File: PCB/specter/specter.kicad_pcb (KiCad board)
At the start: 4 copper layers, 65 x 84.5 mm, 114 parts, among them J1 USB_C_Receptacle_USB2.0_16P, J10 Conn_01x01, J11 Conn_01x01, J13 Conn_01x01, J14 Conn_01x01, J16 Conn_01x01, J17 Conn_01x01, J18 Conn_01x01, J19 Conn_01x01, J2 Micro_SD_Card_Det2, J22 SM04B-SRSS-TB_LF__SN_, J23 Conn_01x01, J24 SM04B-SRSS-TB_LF__SN_, J25 SM04B-SRSS-TB_LF__SN_, J26 SM04B-SRSS-TB_LF__SN_, J27 SM06B-SRSS-TB_LF__SN_, J28 SM06B-SRSS-TB_LF__SN_, J29 SM06B-SRSS-TB_LF__SN_, J3 Bus_M.2_Socket_M, J30 SM06B-SRSS-TB_LF__SN_, J4 Conn_01x22_Socket, J5 Conn_01x22_Socket, J6 Conn_02x01, J7 Conn_01x03, J8 Conn_01x01, J9 Conn_02x01, U1 FT232RL, U10 ASEK-32.768KHZ-L-R-T, U2 FT232RL, U3 RT9742GGJ5, U4 MagJack-A70-112-331N126, U5 TPD4EUSB30, U6 TPD4EUSB30, U7 74LVC1G07_copy, U8 AP2553W6, U9 AP3441SHE-7B

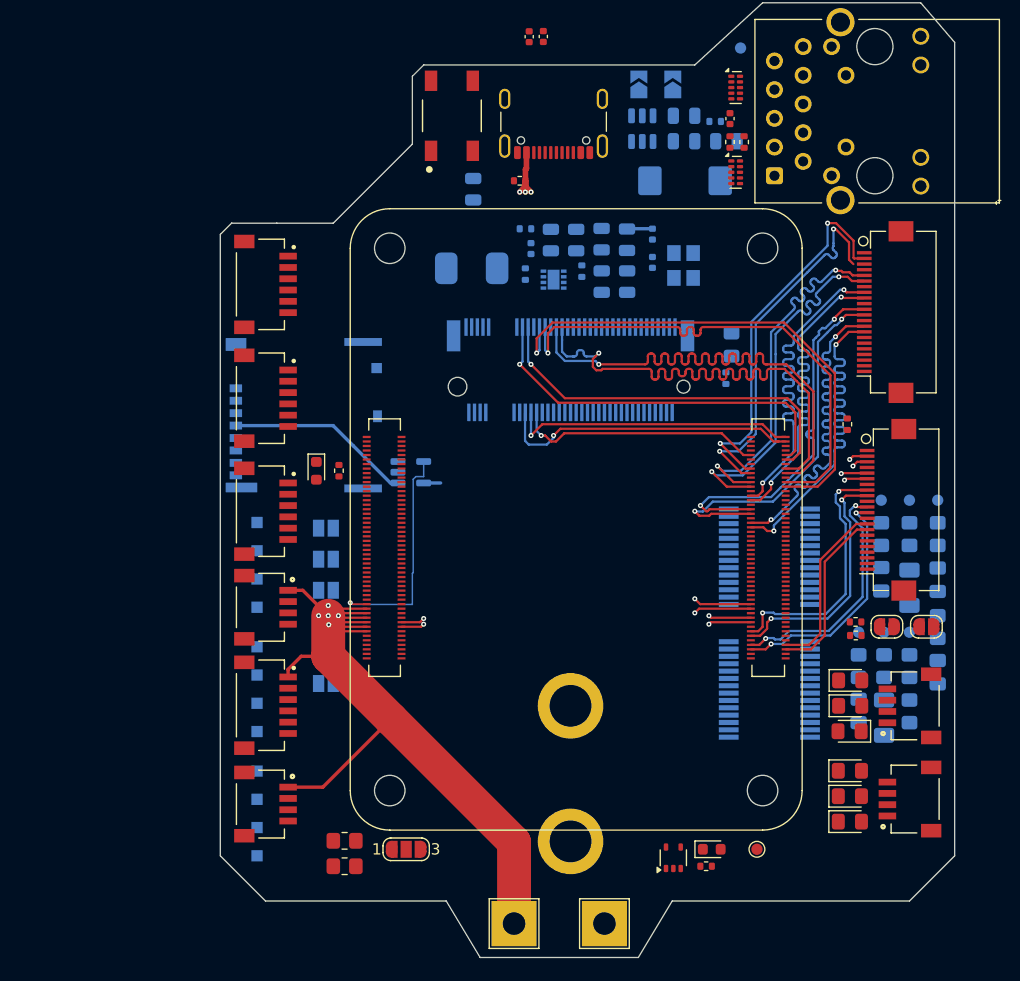
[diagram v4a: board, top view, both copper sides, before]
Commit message: impedance matching
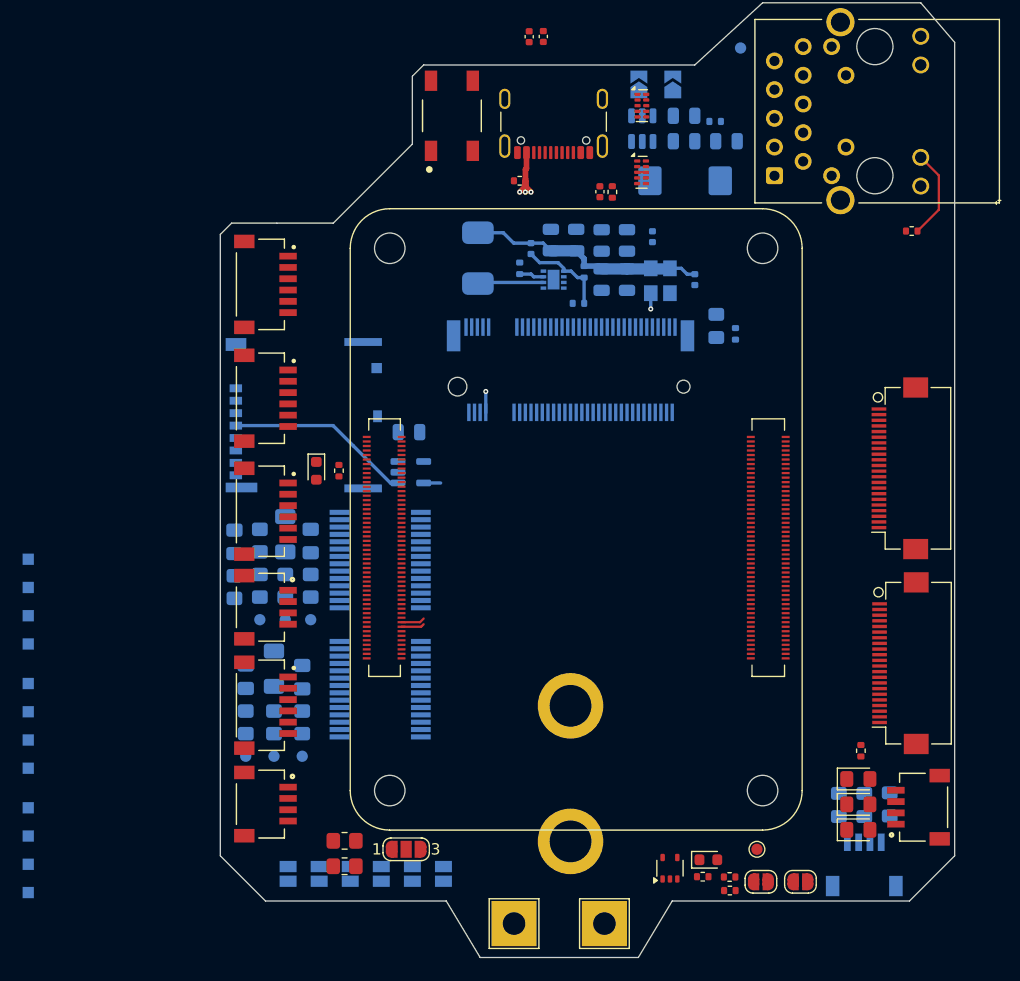
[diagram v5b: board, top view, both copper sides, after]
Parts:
- D1, D2, D3, J24: moved to B.Cu
- moved TP2 65.3 mm to (102.2, 117.2), turned to 180 degrees
- moved R2 63.5 mm to (102.2, 114.2), turned to 90 degrees
- moved C6 63.3 mm to (101.2, 98.2), turned to -90 degrees
- moved R5 62.4 mm to (101.2, 102.2), turned to -90 degrees
- moved C4 61.8 mm to (102.2, 110.2), turned to -90 degrees
- moved TP1 60.6 mm to (104.8, 117.2), turned to 180 degrees
- moved R7 59.5 mm to (103.5, 98.1), turned to -90 degrees
- moved R3 58.7 mm to (104.8, 114.2), turned to -90 degrees
- moved R8 57.9 mm to (103.5, 102.1), turned to -90 degrees
- moved TP5 57.5 mm to (103.5, 105.1), turned to -90 degrees
- moved C5 56.7 mm to (104.8, 109.4), turned to 90 degrees
- moved TP3 56.0 mm to (107.2, 117.2), turned to 180 degrees
- moved C7 55.4 mm to (105.8, 97.5), turned to 90 degrees
- moved R4 53.9 mm to (107.2, 114.2), turned to -90 degrees
- moved R9 53.5 mm to (105.8, 102.1), turned to 90 degrees
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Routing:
- net /+5v: track 85.2 -> 5.95 mm, vias 8 -> 3
- net /PCIE_RX_N: track 48.6 -> 0.00 mm, vias 1 -> 0
- net /PCIE_RX_P: track 48.5 -> 0.00 mm, vias 1 -> 0
- net /PCIE_TX_N: track 46.0 -> 0.00 mm, vias 1 -> 0
- net /PCIE_TX_P: track 46.0 -> 0.00 mm, vias 1 -> 0
- net /PCIE_CLK_N: track 34.1 -> 0.00 mm, vias 1 -> 0
- net /PCIE_CLK_P: track 34.0 -> 0.00 mm, vias 1 -> 0
- net /DPHY0_D0_N: track 33.5 -> 0.00 mm, vias 2 -> 0
- net /DPHY0_D0_P: track 33.5 -> 0.00 mm, vias 2 -> 0
- net /DPHY0_D2_N: track 33.4 -> 0.00 mm, vias 2 -> 0
- net /DPHY0_D2_P: track 33.4 -> 0.00 mm, vias 2 -> 0
- net /DPHY0_D3_P: track 33.3 -> 0.00 mm, vias 2 -> 0
- net /DPHY0_D3_N: track 33.1 -> 0.00 mm, vias 2 -> 0
- net /DPHY0_D1_P: track 33.1 -> 0.00 mm, vias 2 -> 0
- net /DPHY0_D1_N: track 33.0 -> 0.00 mm, vias 2 -> 0
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
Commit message: updated PCB
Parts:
- U5, U6: moved to B.Cu
- moved U8 27.0 mm to (156.3, 80.8), turned to 180 degrees
- moved C14 22.5 mm to (160.9, 77.1), turned to 90 degrees
- moved C13 21.8 mm to (155.1, 77.2), turned to 90 degrees
- moved C12 21.8 mm to (157.4, 77.2), turned to 90 degrees
- moved TP35 20.9 mm to (129.1, 66.7)
- moved J6 19.8 mm to (156.7, 60.3)
- moved R18 17.9 mm to (155.6, 74.4), turned to -90 degrees
- moved C11 15.5 mm to (157.4, 71.8), turned to -90 degrees
- moved J9 14.3 mm to (154.1, 60.3)
- moved C1 14.2 mm to (123.3, 66.7), turned to 90 degrees
- moved C2 13.5 mm to (124.5, 66.7), turned to 90 degrees
- moved U6 10.1 mm to (145.8, 60.0), turned to 180 degrees
- moved U5 9.14 mm to (145.8, 56.2), turned to 180 degrees
- moved C10 1.40 mm to (132.2, 67.2)
- moved R11 1.40 mm to (133.3, 67.2)
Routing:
- net /PCIE_CLK_P: track 0.00 -> 36.4 mm, vias 0 -> 1
- net /PCIE_CLK_N: track 0.00 -> 36.2 mm, vias 0 -> 1
- net /PCIE_RX_N: track 0.00 -> 35.5 mm, vias 0 -> 1
- net /PCIE_RX_P: track 0.00 -> 35.0 mm, vias 0 -> 1
- net /PCIE_nWAKE: track 0.00 -> 33.4 mm, vias 0 -> 2
- net /PCIE_TX_N: track 0.00 -> 32.7 mm, vias 0 -> 1
- net /PCIE_TX_P: track 0.00 -> 32.7 mm, vias 0 -> 1
- net /PCIE_nCLKREQ: track 0.00 -> 30.4 mm, vias 0 -> 1
- net /PCIE_nRST: track 0.00 -> 21.7 mm, vias 0 -> 1
- net Net-(J3-SUSCLK): track 20.9 -> 0.00 mm, vias 2 -> 0
- net /DPHY0_D3_P: track 0.00 -> 17.8 mm, vias 0 -> 2
- net /DPHY0_D3_N: track 0.00 -> 17.8 mm, vias 0 -> 2
- net /DPHY0_D0_P: track 0.00 -> 17.7 mm, vias 0 -> 2
- net /DPHY0_D0_N: track 0.00 -> 17.7 mm, vias 0 -> 2
- net /DPHY0_D1_P: track 0.00 -> 17.5 mm, vias 0 -> 2
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
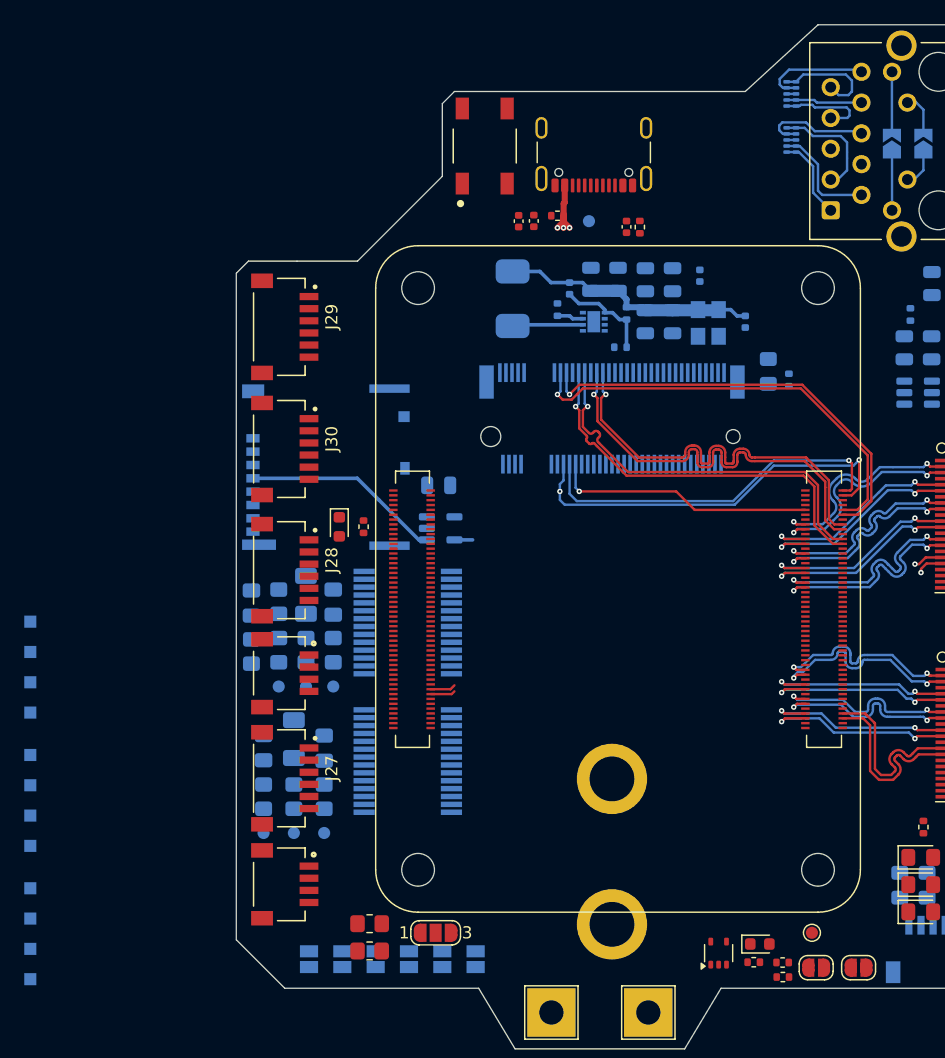
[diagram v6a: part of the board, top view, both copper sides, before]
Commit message: added SD card routing
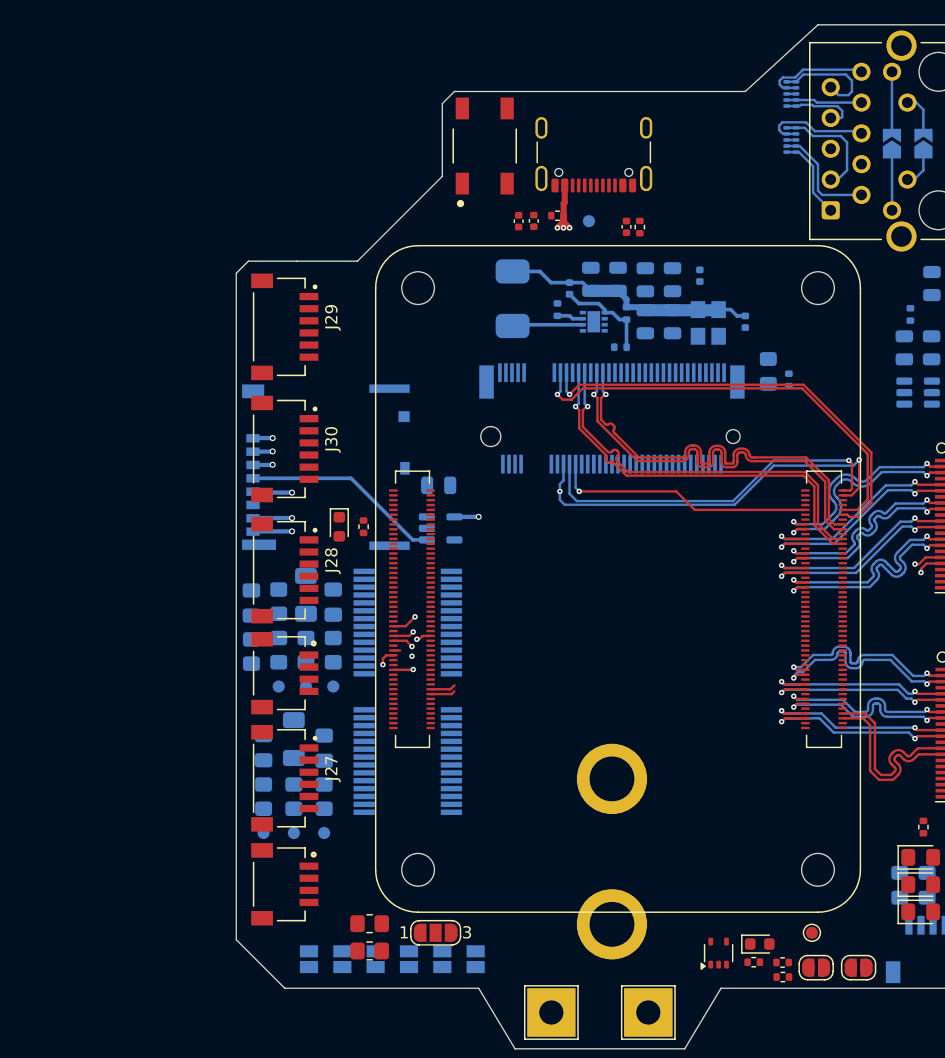
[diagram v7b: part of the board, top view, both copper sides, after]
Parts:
- removed J10, J11, J13 (x5), J14, J16, J17, J18, J19: Conn_01x01, TestPoint:TestPoint_Pad_1.0x1.0mm
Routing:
- net /SD_DAT1: track 0.00 -> 30.9 mm, vias 0 -> 2
- net /SD_DAT2: track 0.00 -> 30.6 mm, vias 0 -> 2
- net /SD_CMD: track 0.00 -> 30.4 mm, vias 0 -> 2
- net /SD_DAT3: track 0.00 -> 23.3 mm, vias 0 -> 2
- net /SD_CLK: track 0.00 -> 21.4 mm, vias 0 -> 2
- net /SD_DAT0: track 0.00 -> 20.6 mm, vias 0 -> 2
- net /SD_PWR_ON: track 0.00 -> 20.0 mm, vias 0 -> 2
- net /+3.3v: track 5.65 -> 4.15 mm
- net /TRD2_P: track 7.92 -> 6.75 mm

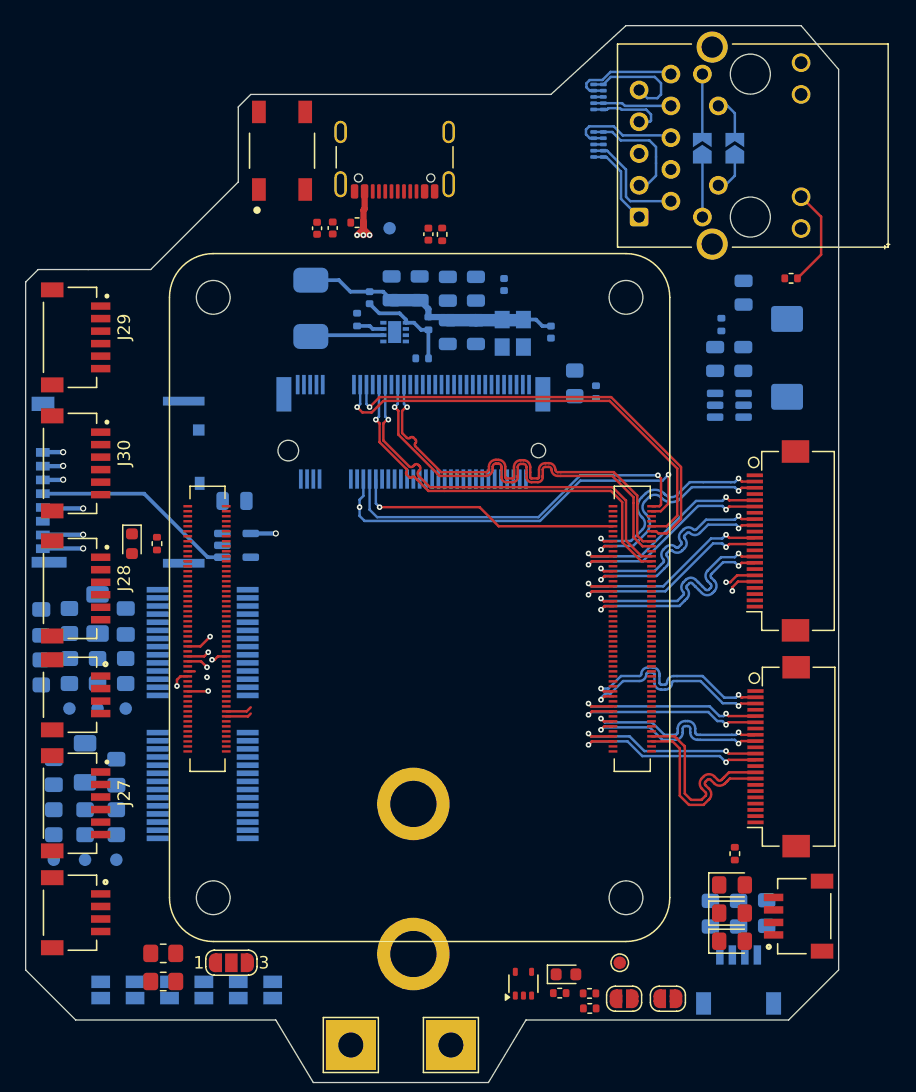
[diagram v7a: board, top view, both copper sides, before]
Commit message: GPIO wired
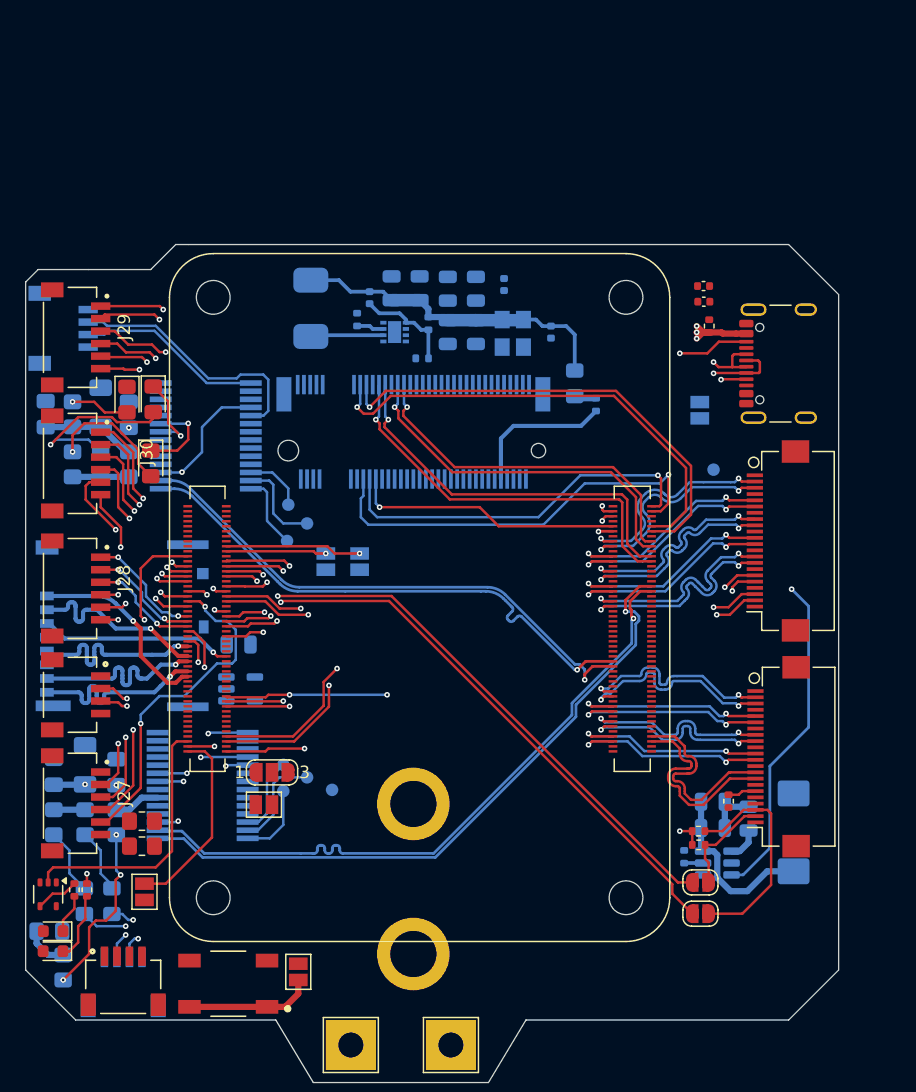
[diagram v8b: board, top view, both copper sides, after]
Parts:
- removed C10: 100nF, Capacitor_SMD:C_0402_1005Metric
- removed J6, J9: Conn_02x01, Jumper:SolderJumper-2_P1.3mm_Open_TrianglePad1.0x1.5mm
- removed R10, R11: 470R, Resistor_SMD:R_0402_1005Metric
- removed U4: MagJack-A70-112-331N126, CM5IO:TRJG0926HENL
- removed U5, U6: TPD4EUSB30, Package_SON:USON-10_2.5x1.0mm_P0.5mm
- J25, TP33: moved to B.Cu
- JP1, JP5, JP6: moved to F.Cu
- moved J25 72.2 mm to (105.0, 74.7)
- moved S1 66.7 mm to (116.2, 127.1), turned to 180 degrees
- moved D6 63.4 mm to (110.2, 80.4), turned to -90 degrees
- moved D4 62.0 mm to (108.1, 80.4), turned to -90 degrees
- moved D5 58.8 mm to (110.0, 85.5), turned to -90 degrees
- moved JP4 57.6 mm to (153.9, 81.2), turned to -90 degrees
- moved D3 57.4 mm to (101.9, 122.9), turned to 180 degrees
- moved D1 52.3 mm to (104.7, 120.5), turned to 90 degrees
- moved J24 49.2 mm to (107.8, 125.0)
- moved D2 47.9 mm to (106.9, 120.5), turned to 90 degrees
- moved R18 42.7 mm to (152.7, 117.0), turned to 90 degrees
- moved C11 42.1 mm to (157.8, 113.9), turned to 90 degrees
- moved D7 41.1 mm to (102.2, 122.9), turned to 180 degrees
- moved JP3 40.0 mm to (126.7, 93.3)
- moved R17 39.7 mm to (103.9, 119.6), turned to 90 degrees
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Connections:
- J28 pad 1: /GPIO4 -> /GPIO24
- J28 pad 2: /GPIO5 -> /GPIO23
- J28 pad 3: /GPIO6 -> /GPIO18
- J28 pad 4: /GPIO7 -> /GPIO22
- J28 pad 5: /GPIO12 -> /GPIO27
- J28 pad 6: /GPIO13 -> /GPIO17
- J29 pad 1: /GPIO16 -> /GPIO26
- J29 pad 2: /GPIO17 -> /GPIO19
- J29 pad 3: /GPIO18 -> /GPIO13
- J29 pad 4: /GPIO19 -> /GPIO6
- J29 pad 5: /GPIO20 -> /GPIO5
- J29 pad 6: /GPIO21 -> /GPIO4
- J30 pad 1: /GPIO22 -> /GPIO21
- J30 pad 2: /GPIO23 -> /GPIO20
- J30 pad 3: /GPIO24 -> /GPIO16
- J30 pad 4: /GPIO25 -> /GPIO12
- J30 pad 5: /GPIO26 -> /GPIO7
- J30 pad 6: /GPIO27 -> /GPIO25
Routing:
- net /CC1: track 0.00 -> 58.0 mm, vias 0 -> 2
- net /CC2: track 0.00 -> 55.8 mm, vias 0 -> 2
- net /USB3-0-D_P: track 0.00 -> 53.5 mm, vias 0 -> 1
- net /USB3-0-D_N: track 0.00 -> 53.5 mm, vias 0 -> 1
- net /ID_SC: track 0.00 -> 51.5 mm, vias 0 -> 2
- net /CAM_GPIO0: track 2.53 -> 52.7 mm, vias 1 -> 2
- net /ID_SD: track 0.00 -> 49.2 mm, vias 0 -> 2
- net /CAM_GPIO1: track 2.29 -> 49.6 mm, vias 1 -> 2
- net /SCL0: track 0.00 -> 45.8 mm, vias 0 -> 2
- net /SDA0: track 0.00 -> 45.8 mm, vias 0 -> 2
- net /VBUS_EN: track 0.00 -> 45.2 mm, vias 0 -> 2
- net /USB3-1-D_N: track 0.00 -> 43.7 mm, vias 0 -> 1
- net /USB3-1-D_P: track 0.00 -> 43.6 mm, vias 0 -> 1
- net /GPIO_VREF: track 0.00 -> 43.0 mm, vias 0 -> 3
- net /GPIO4: track 0.00 -> 35.4 mm, vias 0 -> 2
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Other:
- board size 65 x 84.5 mm -> 65 x 67 mm
